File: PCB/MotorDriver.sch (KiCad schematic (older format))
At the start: 5 parts, among them U5 DRV8871DDA

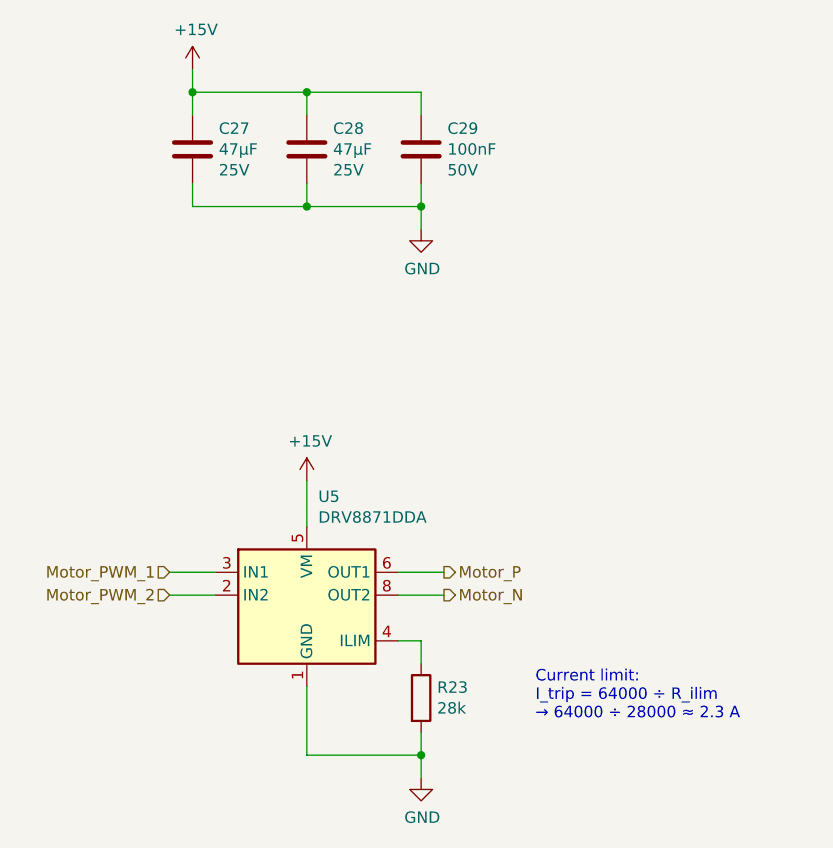
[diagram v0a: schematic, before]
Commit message: Add jumpers on the power supply outputs
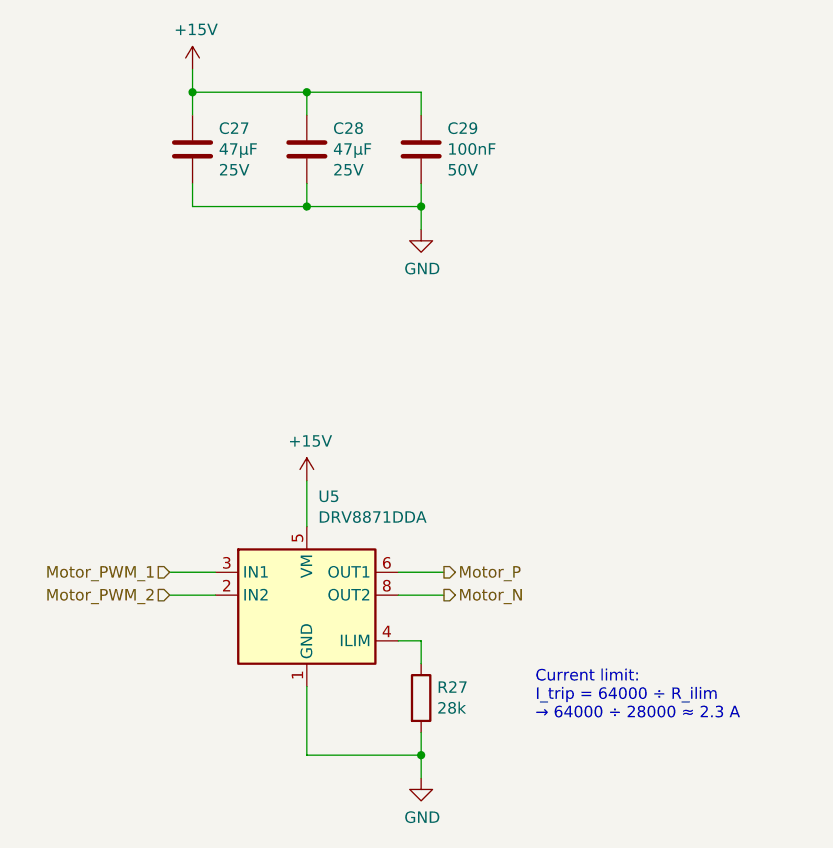
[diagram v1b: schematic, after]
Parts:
- renumbered R23 to R27
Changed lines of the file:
@@
 Sheet 8 23
 Title "Litter Robot 3 - Motor driver"
-Date "2021-04-10"
+Date "2021-05-24"
 Rev "A1"
 Comp "L. Sartory"
@@
 	6000 4400 6000 4500
 $Comp
-L Device:R R23
+L Device:R R27
 U 1 1 604667F9
 P 6000 4650
-F 0 "R23" H 6070 4696 50  0000 L CNN
+F 0 "R27" H 6070 4696 50  0000 L CNN
 F 1 "28k" H 6070 4605 50  0000 L CNN
 F 2 "Resistor_SMD:R_0603_1608Metric" V 5930 4650 50  0001 C CNN
